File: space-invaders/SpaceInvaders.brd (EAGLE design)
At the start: 127 x 101.6 mm, 26 parts, among them J1 9V, J2_J4 TM4C123GXL, J3_J1 TM4C123GXL, J5 Nokia 5110, J6 Nokia 5110, U1 5V Voltage Regulator

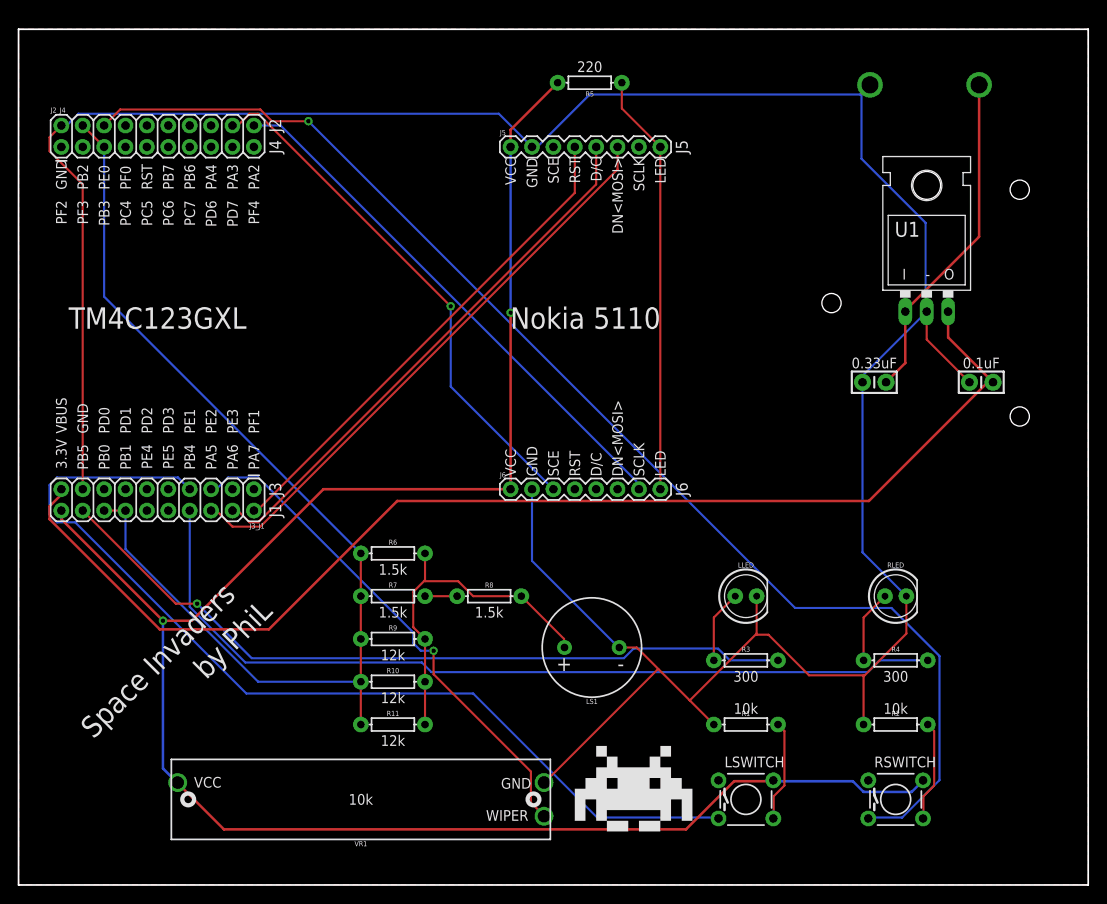
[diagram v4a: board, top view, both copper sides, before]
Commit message: Reposition SpaceInvaders board layout
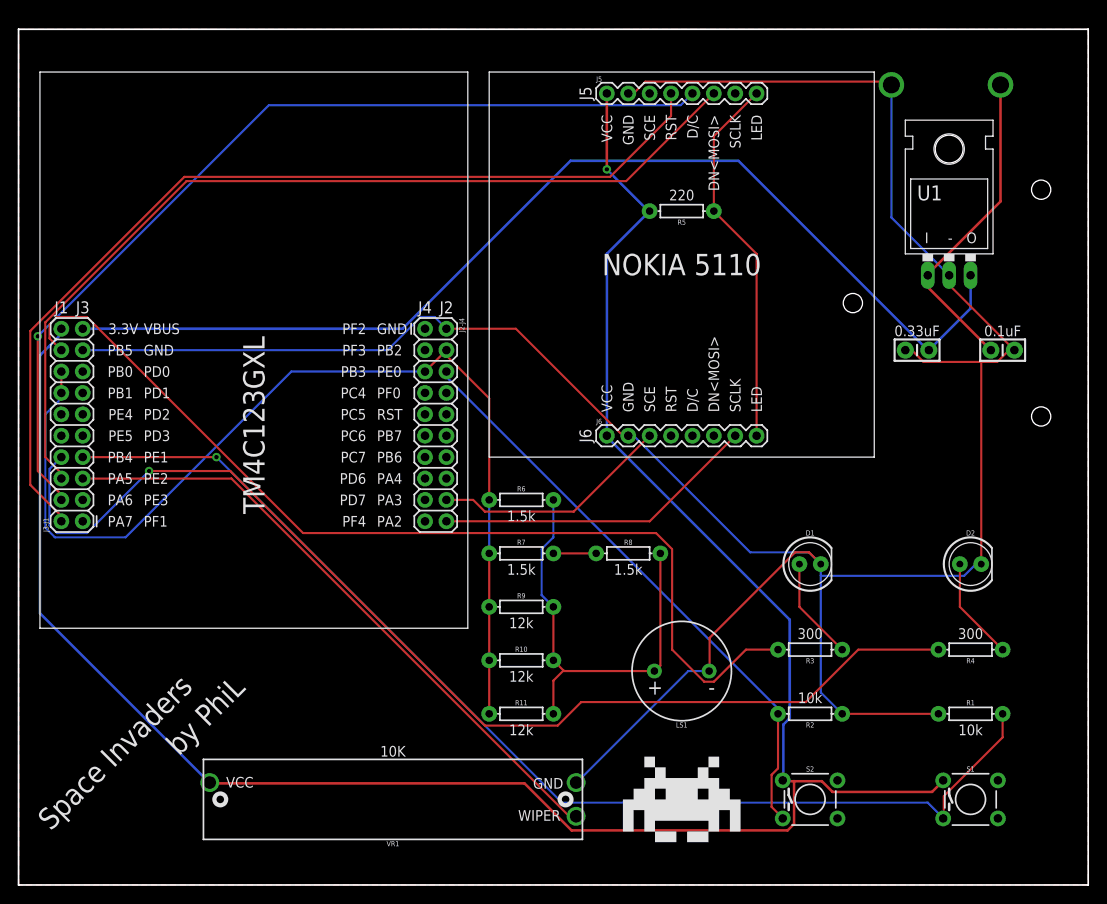
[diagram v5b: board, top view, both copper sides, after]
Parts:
- removed J1: 9V, SparkFun-Connectors:BC9VPC
- removed J2_J4, J3_J1: TM4C123GXL, SparkFun-Connectors:2X10
- removed LLED: YELLOW, SparkFun-LED:LED_5MM
- removed LSWITCH, RSWITCH: TACTILE, SparkFun-Retired:TACTILE-PTH
- removed RLED: RED, SparkFun-LED:LED_5MM
- added D1: YELLOW, SparkFun-LED:LED_5MM
- added D2: RED, SparkFun-LED:LED_5MM
- added J2-J4, J3-J1: TM4C123GXL, SparkFun-Connectors:2X10
- added J7: 9V, SparkFun-Connectors:BC9VPC
- added S1: SPECIAL, SparkFun-Switches:TACTILE_SWITCH_PTH_6.0MM
- added S2: REGULAR, SparkFun-Switches:TACTILE_SWITCH_PTH_6.0MM
- C1: value 0.1μF -> 0.1uF
- C2: value 0.33μF -> 0.33uF
- J5, J6: value Nokia 5110 -> Nokia_5110
- LS1: value BUZZER-PTH -> BUZZER
- R1, R2, VR1: value 10kΩ -> 10k
- R10, R11, R9: value 12kΩ -> 12k
- R3, R4: value 300Ω -> 300
- R5: value 220Ω -> 220
- R6, R7, R8: value 1.5kΩ -> 1.5k
- U1: value 5V Voltage Regulator -> LM7805CT
- moved R1 26.7 mm to (113.0, 20.3)
- moved R5 18.7 mm to (78.7, 80.0)
- moved R8 17.3 mm to (72.4, 39.4)
- moved R6 16.5 mm to (59.7, 45.7)
- moved R7 16.1 mm to (59.7, 39.4)
- moved C2 15.7 mm to (116.8, 63.5), turned to 0 degrees
- moved R9 15.7 mm to (59.7, 33.0)
- moved R10 15.5 mm to (59.7, 26.7)
- moved R11 15.3 mm to (59.7, 20.3)
- moved J5 13.1 mm to (69.8, 94.0)
- moved J6 13.1 mm to (69.8, 53.3)
- moved LS1 11.0 mm to (78.7, 25.4)
- moved R2 10.2 mm to (94.0, 20.3), turned to 180 degrees
- moved R4 8.98 mm to (113.0, 27.9), turned to 180 degrees
- moved C1 8.52 mm to (106.7, 63.5)
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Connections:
- removed net LSWITCH_GND: LSWITCH.4, R1.P$2
- removed net RSWITCH_GND: R2.P$2, RSWITCH.4
- net 3.3V: now also J3-J1.20, S1.1, S2.1; no longer J3_J1.20, LSWITCH.2, RSWITCH.2
- net 9V: now also J7.V+; no longer J1.V+
- net GND: now also D1.K, D2.K, J2-J4.2, J3-J1.17, J7.V-; no longer J1.V-, J2_J4.2, J3_J1.17, LLED.K, RLED.K
- net LLED: now also D1.A; no longer LLED.A
- net PA2: now also J2-J4.20; no longer J2_J4.20
- net PA3: now also J2-J4.18; no longer J2_J4.18
- net PA4: now also J2-J4.16; no longer J2_J4.16
- net PA5: now also J3-J1.6; no longer J3_J1.6
- net PA6: now also J3-J1.4; no longer J3_J1.4
- net PA7: now also J3-J1.2; no longer J3_J1.2
- net PB2: now also J2-J4.4, J2-J4.5, J3-J1.14, J3-J1.16; no longer J2_J4.4, J2_J4.5, J3_J1.14, J3_J1.16
- net PB4: now also J3-J1.8; no longer J3_J1.8
- net PB5: now also J3-J1.18; no longer J3_J1.18
- net PB6: now also J2-J4.14; no longer J2_J4.14
- net PB7: now also J2-J4.12; no longer J2_J4.12
- net PC4: now also J2-J4.7; no longer J2_J4.7
- net PC5: now also J2-J4.9; no longer J2_J4.9
- net PC6: now also J2-J4.11; no longer J2_J4.11
- net PC7: now also J2-J4.13; no longer J2_J4.13
- net PD0: now also J3-J1.15; no longer J3_J1.15
- net PD1: now also J3-J1.13; no longer J3_J1.13
- net PD2: now also J3-J1.11; no longer J3_J1.11
- net PD3: now also J3-J1.9; no longer J3_J1.9
- net PD6: now also J2-J4.15; no longer J2_J4.15
- net PD7: now also J2-J4.17; no longer J2_J4.17
- net PE0: now also J2-J4.6, R2.P$2, S2.3; no longer J2_J4.6, RSWITCH.3
- net PE1: now also J3-J1.7, R1.P$2, S1.3; no longer J3_J1.7, LSWITCH.3
- net PE2: now also J3-J1.5; no longer J3_J1.5
- net PE3: now also J3-J1.3; no longer J3_J1.3
- net PE4: now also J3-J1.12; no longer J3_J1.12
- net PE5: now also J3-J1.10; no longer J3_J1.10
- net PF0: now also J2-J4.8; no longer J2_J4.8
- net PF1: now also J3-J1.1; no longer J3_J1.1
- net PF2: now also J2-J4.1; no longer J2_J4.1
- net PF3: now also J2-J4.3; no longer J2_J4.3
- net PF4: now also J2-J4.19; no longer J2_J4.19
- net RESET: now also J2-J4.10; no longer J2_J4.10
- net RLED: now also D2.A; no longer RLED.A
- net VBUS: now also J3-J1.19; no longer J3_J1.19
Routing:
- net PE0: track 151.9 -> 70.2 mm, vias 1 -> 0
- net PA7: track 59.2 -> 113.4 mm
- net PA6: track 64.8 -> 110.3 mm, vias 0 -> 1
- net PA5: track 69.3 -> 110.0 mm
- net PA3: track 62.7 -> 28.4 mm, vias 1 -> 0
- net PB4: track 102.8 -> 133.9 mm, vias 0 -> 1
- net GND: track 330.6 -> 302.4 mm
- net PB5: track 90.9 -> 117.0 mm, vias 1 -> 0
- net PA2: track 64.0 -> 38.5 mm
- net 3.3V: track 230.8 -> 255.9 mm, vias 2 -> 1
- net PE1: track 115.5 -> 135.3 mm, vias 0 -> 1
- net VBUS: track 144.5 -> 129.0 mm
- net PE2: track 61.3 -> 75.2 mm, vias 1 -> 0
- net RSWITCH_GND: track 12.0 -> 0.00 mm
- net LSWITCH_GND: track 12.0 -> 0.00 mm
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- added copper zone on layer 1, net GND
- removed copper zone on layer 1, net N$2
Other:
- board text added: "10K"
- board text added: "NOKIA 5110"
- board text removed: "Nokia 5110"

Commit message: Finish SpaceInvaders v2.0 for manufacturing
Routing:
- net PB2: track 122.1 -> 140.9 mm
- net 3.3V: track 255.9 -> 272.4 mm, vias 1 -> 0
- net PA7: track 113.4 -> 98.1 mm, vias 0 -> 1
- net PE0: track 70.2 -> 83.0 mm
- net PB5: track 117.0 -> 125.7 mm
- net VBUS: track 129.0 -> 121.4 mm
- net 9V: track 38.2 -> 44.3 mm
- net LLED: track 12.3 -> 17.6 mm
- net PB4: track 133.9 -> 129.5 mm, vias 1 -> 0
- net PA5: track 110.0 -> 114.4 mm
- net GND: track 302.4 -> 298.8 mm
- net PE1: track 135.3 -> 138.3 mm, vias 1 -> 0
- net RLED: track 12.3 -> 14.1 mm
- net PA6: track 110.3 -> 112.1 mm
- net PA3: track 28.4 -> 27.3 mm
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
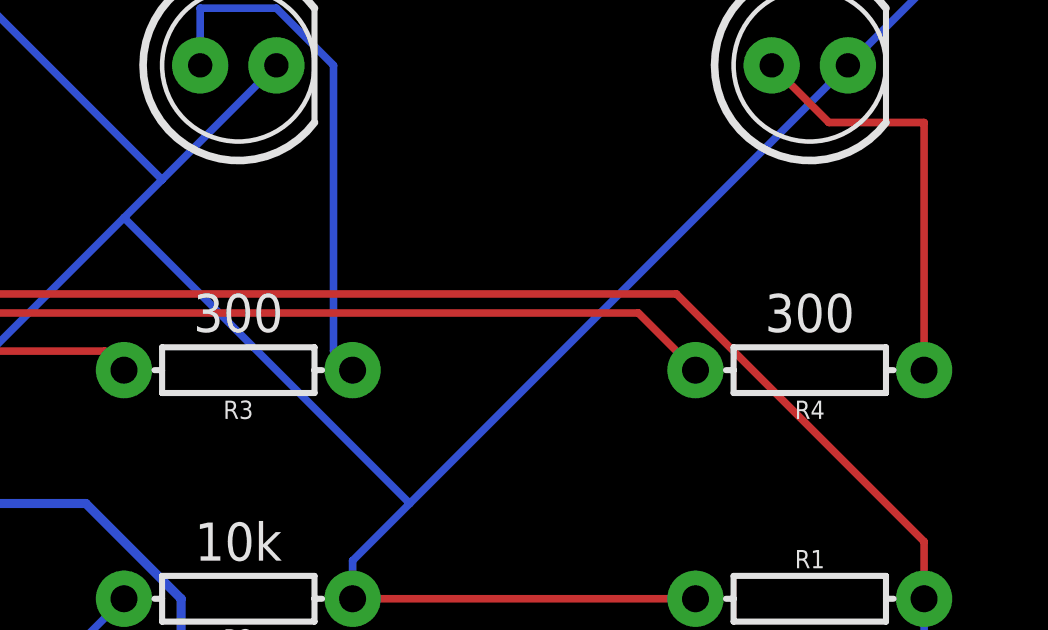
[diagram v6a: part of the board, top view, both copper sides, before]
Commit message: Change LLED and RLED resistor value from 300 to 220
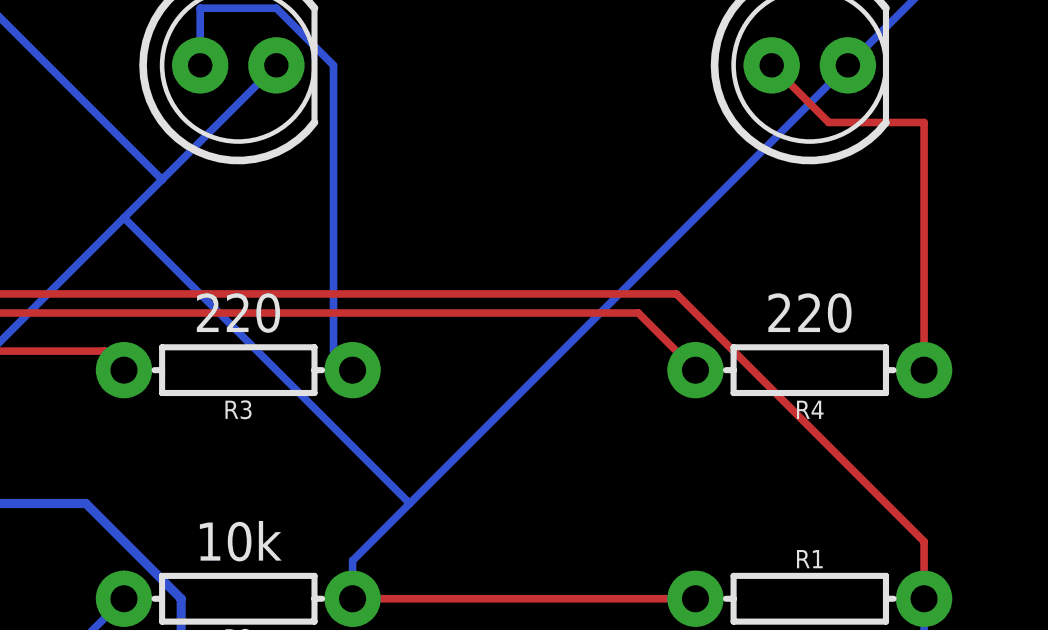
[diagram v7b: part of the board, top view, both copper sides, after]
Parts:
- D1: value YELLOW -> RED
- D2: value RED -> YELLOW
- R3, R4: value 300 -> 220
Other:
- board text removed: "300"
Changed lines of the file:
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@@
 <text x="110.617" y="76.835" size="1.27" layer="21" font="vector" ratio="10" align="center">-</text>
 <text x="78.74" y="82.55" size="1.27" layer="21" font="vector" align="top-center">220</text>
-<text x="93.98" y="30.48" size="1.27" layer="21" font="vector" align="top-center">300</text>
-<text x="113.03" y="30.48" size="1.27" layer="21" font="vector" align="top-center">300</text>
+<text x="93.98" y="30.48" size="1.27" layer="21" font="vector" align="top-center">220</text>
+<text x="113.03" y="30.48" size="1.27" layer="21" font="vector" align="top-center">220</text>
 <text x="93.98" y="21.59" size="1.27" layer="21" font="vector" rot="R180" align="top-center">10k</text>
 <text x="113.03" y="17.78" size="1.27" layer="21" font="vector" rot="R180" align="top-center">10k</text>
@@
 <attribute name="PROD_ID" value="CAP-08370" x="116.84" y="63.5" size="1.778" layer="27" display="off"/>
 </element>
-<element name="D1" library="SparkFun-LED" package="LED_5MM" value="YELLOW" x="93.98" y="38.1"/>
-<element name="D2" library="SparkFun-LED" package="LED_5MM" value="RED" x="113.03" y="38.1"/>
+<element name="D1" library="SparkFun-LED" package="LED_5MM" value="RED" x="93.98" y="38.1"/>
+<element name="D2" library="SparkFun-LED" package="LED_5MM" value="YELLOW" x="113.03" y="38.1"/>
 <element name="FRAME1" library="SparkFun-Aesthetics" package="CREATIVE_COMMONS" value="FRAME-LETTER" x="30.48" y="-8.89"/>
 <element name="J2-J4" library="SparkFun-Connectors" package="2X10" value="TM4C123GXL" x="48.26" y="66.04" rot="R270"/>
@@
 <attribute name="PROD_ID" value="RES-09435" x="93.98" y="20.32" size="1.778" layer="27" rot="R180" display="off"/>
 </element>
-<element name="R3" library="SparkFun-Resistors" package="AXIAL-0.3" value="300" x="93.98" y="27.94" rot="R180">
+<element name="R3" library="SparkFun-Resistors" package="AXIAL-0.3" value="220" x="93.98" y="27.94" rot="R180">
 <attribute name="PROD_ID" value="RES-08380" x="93.98" y="27.94" size="1.778" layer="27" rot="R180" display="off"/>
 </element>
-<element name="R4" library="SparkFun-Resistors" package="AXIAL-0.3" value="300" x="113.03" y="27.94" rot="R180">
+<element name="R4" library="SparkFun-Resistors" package="AXIAL-0.3" value="220" x="113.03" y="27.94" rot="R180">
 <attribute name="PROD_ID" value="RES-08380" x="113.03" y="27.94" size="1.778" layer="27" rot="R180" display="off"/>
 </element>

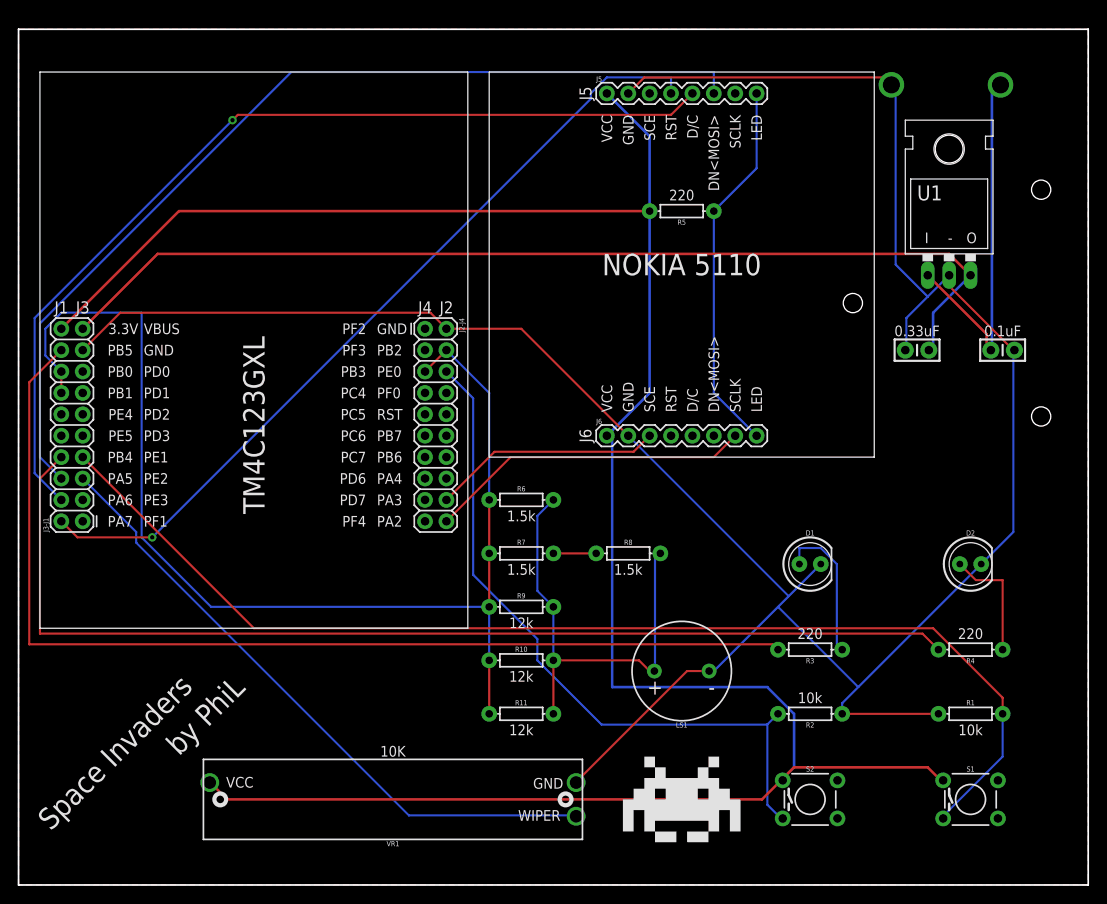
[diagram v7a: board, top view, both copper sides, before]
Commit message: Minimize the size of SpaceInvaders
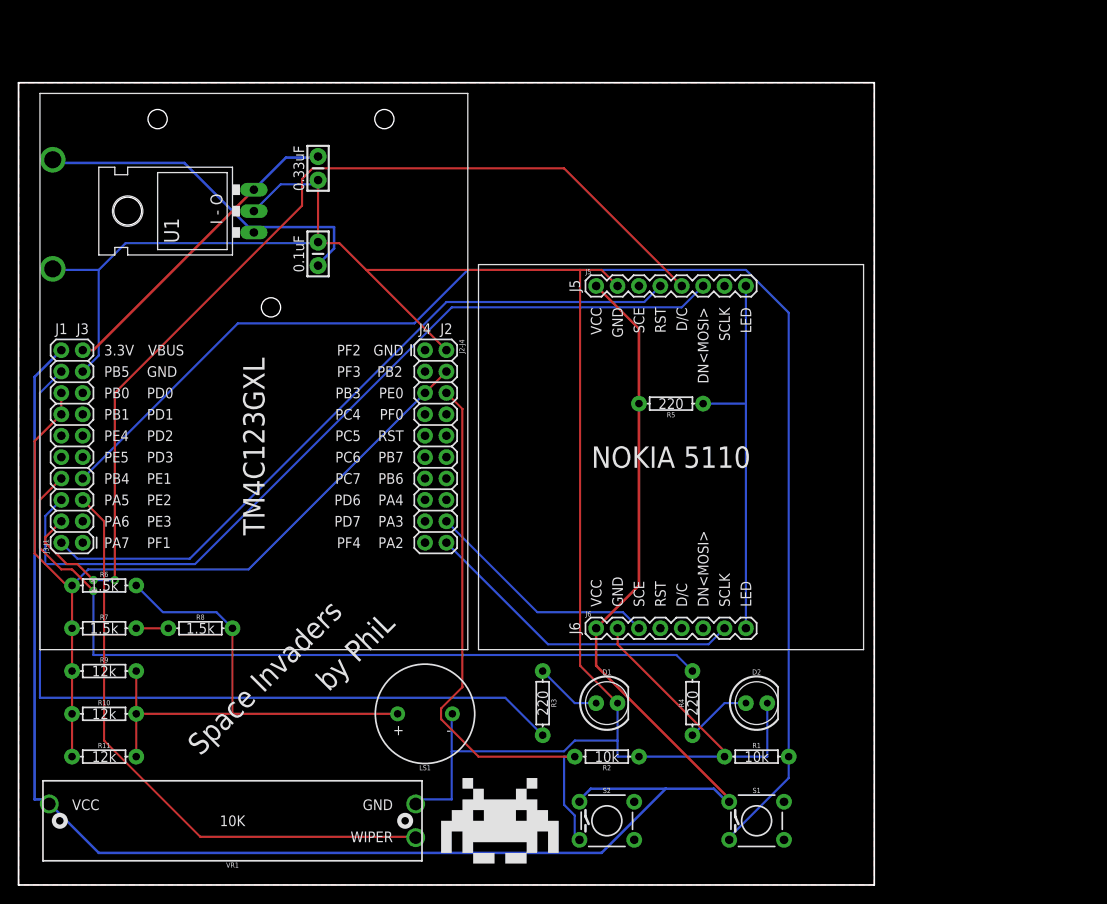
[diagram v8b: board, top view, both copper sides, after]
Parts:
- moved U1 86.4 mm to (24.1, 80.0), turned to 90 degrees
- moved C2 82.1 mm to (35.6, 74.9), turned to 90 degrees
- moved C1 74.3 mm to (35.6, 85.1), turned to 90 degrees
- moved R8 51.6 mm to (21.6, 30.5)
- moved R6 50.6 mm to (10.2, 35.6)
- moved R7 50.3 mm to (10.2, 30.5)
- moved R9 50.1 mm to (10.2, 25.4)
- moved R10 49.9 mm to (10.2, 20.3)
- moved R11 49.8 mm to (10.2, 15.2)
- moved J7 44.4 mm to (57.1, 64.8), turned to 0 degrees
- moved R4 33.6 mm to (80.0, 21.6), turned to 90 degrees
- moved R3 32.4 mm to (62.2, 21.6), turned to 270 degrees
- moved LS1 30.9 mm to (48.3, 20.3)
- moved D2 30.3 mm to (87.6, 21.6)
- moved D1 29.2 mm to (69.8, 21.6)
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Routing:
- net VBUS: track 121.4 -> 37.5 mm
- net 3.3V: track 272.4 -> 226.5 mm
- net GND: track 298.8 -> 253.1 mm
- net PB2: track 140.9 -> 101.9 mm
- net PB4: track 129.5 -> 97.3 mm, vias 0 -> 1
- net PB5: track 125.7 -> 101.3 mm
- net PE1: track 138.3 -> 161.7 mm
- net PA5: track 114.4 -> 100.2 mm
- net PA7: track 98.1 -> 85.3 mm, vias 1 -> 0
- net PE0: track 83.0 -> 70.3 mm
- net DAC_OUT: track 53.8 -> 64.9 mm
- net LLED: track 17.6 -> 7.93 mm
- net PA6: track 112.1 -> 121.7 mm, vias 1 -> 2
- net RLED: track 14.1 -> 7.93 mm
- net PE2: track 75.9 -> 71.4 mm
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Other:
- board size 127 x 101.6 mm -> 101.6 x 95.2 mm
- board text added: "I - O"
- board text removed: "I"
- board text removed: "O"
